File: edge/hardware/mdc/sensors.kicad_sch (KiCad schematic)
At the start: 4 parts

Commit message: rev3.0 schematics
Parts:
- U2: value (none) -> INMP441
- U3: value (none) -> GY-906
- U4: value (none) -> STEVAL-MKIGIBV2
- U6: value (none) -> INA219
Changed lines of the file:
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@@
 	(title_block
 		(title "Sensors")
-		(date "2026-08-08")
+		(date "2026-08-09")
 		(rev "3.0")
 		(comment 1 "Department of EECS- AIoT and Energy Management Lab")
@@
 			)
 		)
-		(property "Value" ""
+		(property "Value" "GY-906"
 			(at 64.77 102.87 0)
+			(hide yes)
 			(show_name no)
 			(do_not_autoplace no)
@@
 			)
 		)
-		(property "Value" ""
-			(at 172.72 102.87 0)
+		(property "Value" "INMP441"
+			(at 189.484 110.998 0)
+			(hide yes)
 			(show_name no)
 			(do_not_autoplace no)
@@
 			)
 		)
-		(property "Value" ""
+		(property "Value" "INA219"
 			(at 226.06 102.87 0)
+			(hide yes)
 			(show_name no)
 			(do_not_autoplace no)
@@
 			)
 		)
-		(property "Value" ""
+		(property "Value" "STEVAL-MKIGIBV2"
 			(at 118.11 102.87 0)
-			(show_name no)
-			(do_not_autoplace no)
+			(hide yes)
+			(show_name no)
+			(do_not_autoplace no)

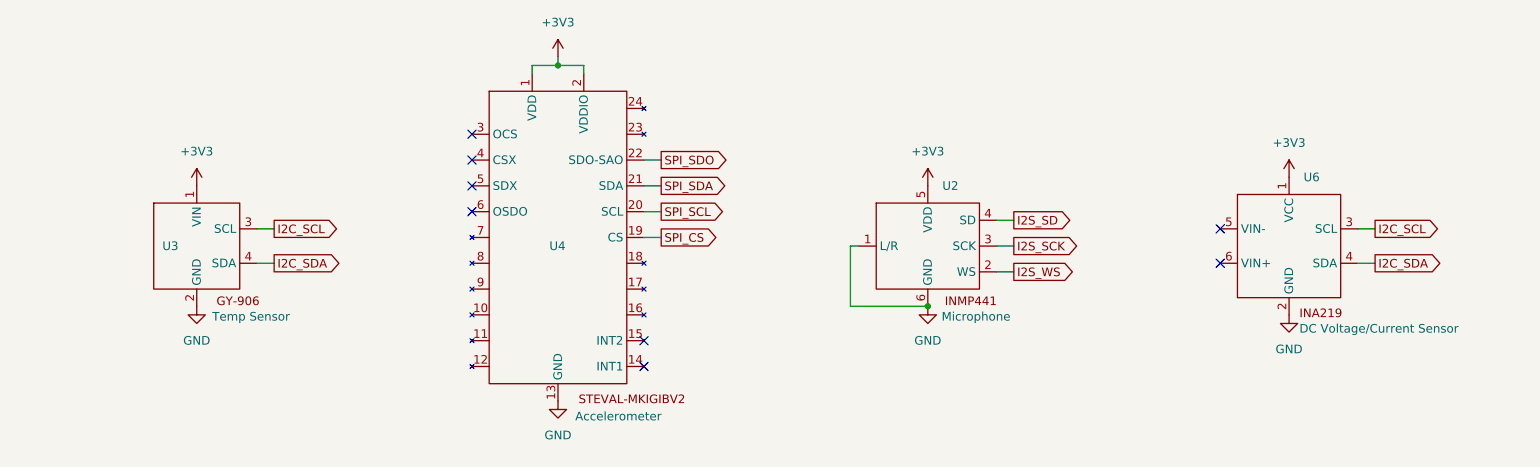
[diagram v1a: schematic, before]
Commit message: finish rev3.0 PCB layout + data collector script changes + firmware changes
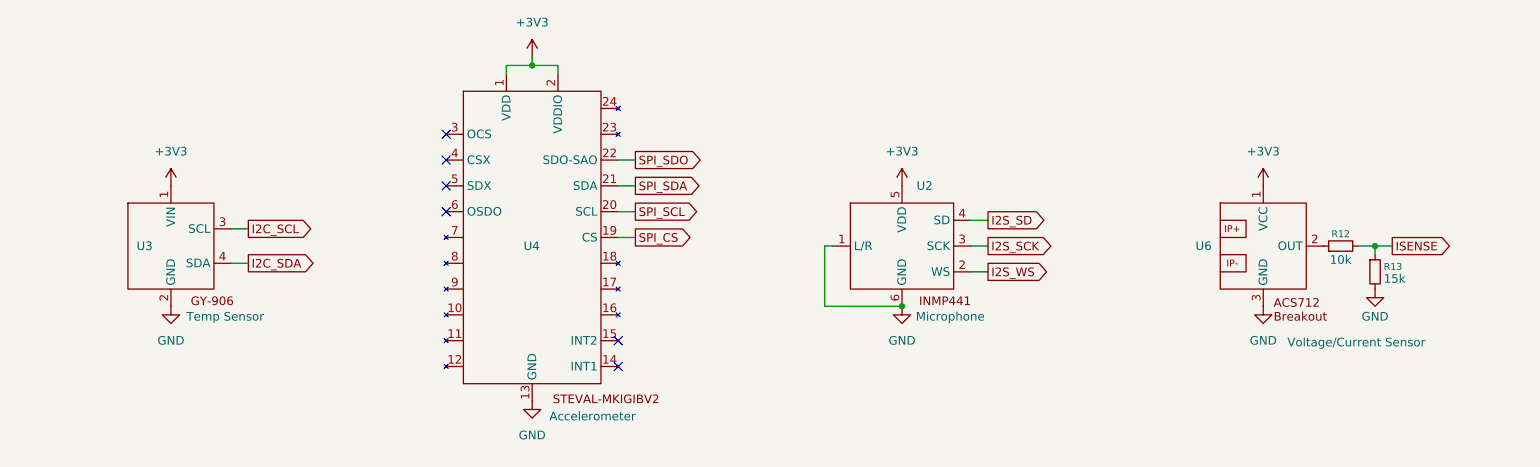
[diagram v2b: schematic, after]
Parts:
- removed U6: INA219, symbol INA219_breakout:INA219_breakout
- added R12: 10k, Resistor_THT:R_Axial_DIN0207_L6.3mm_D2.5mm_P7.62mm_Horizontal, symbol Device:R_Small
- added R13: 15k, Resistor_THT:R_Axial_DIN0207_L6.3mm_D2.5mm_P7.62mm_Horizontal, symbol Device:R_Small
- added U6: ACS712-30A, Connector_PinSocket_2.54mm:PinSocket_1x03_P2.54mm_Vertical, symbol ACS712_breakout:ACS712
- U2: footprint (none) -> Package_DIP:DIP-6_W7.62mm
- U3: footprint (none) -> Connector_PinSocket_2.54mm:PinSocket_1x04_P2.54mm_Vertical
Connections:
- net +3V3: now also U6.1 (VCC)
- net GND: now also R13.2, U6.3 (GND)
- new net: R12.1, U6.2 (OUT)
- new net ISENSE: R12.2, R13.1
- no-connect marks 8 -> 6
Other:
- moved on the sheet: U2, U3, U4

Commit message: update rev3.0 schematic and layout
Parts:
- added C3, C6, C7, C8, C9: 100nF, Capacitor_THT:C_Disc_D5.0mm_W2.5mm_P5.00mm, symbol Device:C_Small
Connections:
- net +3V3: now also C3.1, C8.1, C9.1; no longer U6.1 (VCC)
- net GND: now also C3.2, C6.2, C7.2, C8.2, C9.2
- net ISENSE: now also C6.1
- new net +5V: C7.1, U6.1 (VCC)
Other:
- moved on the sheet: R12, R13, U2, U3, U6
